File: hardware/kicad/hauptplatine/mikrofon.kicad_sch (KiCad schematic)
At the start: 20 parts, among them J601 Mikrofon, U601 TLV9001IDBVR

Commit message: update
Footprints BQ25185, Ra-01SH, DEGSON 15EDGRC-3.5 (2-6P) in Bienen.pretty; HW-02 Akkuhalter Keystone 1042 SMD; SCH26-13 Klemmen einreihig mit LCSC-Nummern. Tests: ERC 0, Pin/Footprint 0 Abweichungen, Netzprüfung 178/178, alle_tests_linux.sh rc=0
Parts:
- J601: footprint Connector_Phoenix_MC:PhoenixContact_MC_1,5_4-G-3.5_1x04_P3.50mm_Horizontal -> Bienen:DEGSON_15EDGRC-3.5-04P; LCSC (none) -> C7603438
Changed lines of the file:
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@@
 			)
 		)
-		(property "Footprint" "Connector_Phoenix_MC:PhoenixContact_MC_1,5_4-G-3.5_1x04_P3.50mm_Horizontal"
+		(property "Footprint" "Bienen:DEGSON_15EDGRC-3.5-04P"
 			(at 38.1 132.08 0)
 			(hide yes)
@@
 			)
 		)
-		(property "Description" "= J5 in anschluesse.md: 1 Schirm, 2 GND, 3 OUT, 4 VCC (3V3_ANA); DEGSON 15EDGRHC-3.5 4-polig C7603445 (Platzhalter-Footprint Phoenix MC) [P]; Schirm nur hier an Masse"
+		(property "Description" "= J5 in anschluesse.md: 1 Schirm, 2 GND, 3 OUT, 4 VCC (3V3_ANA); DEGSON 15EDGRC-3.5-04P; Schirm nur hier an Masse"
 			(at 38.1 132.08 0)
 			(hide yes)
+			(show_name no)
+			(do_not_autoplace no)
+			(effects
+				(font
+					(size 1.27 1.27)
+				)
+			)
+		)
+		(property "LCSC" "C7603438"
+			(at 38.1 132.08 0)
+			(hide yes)

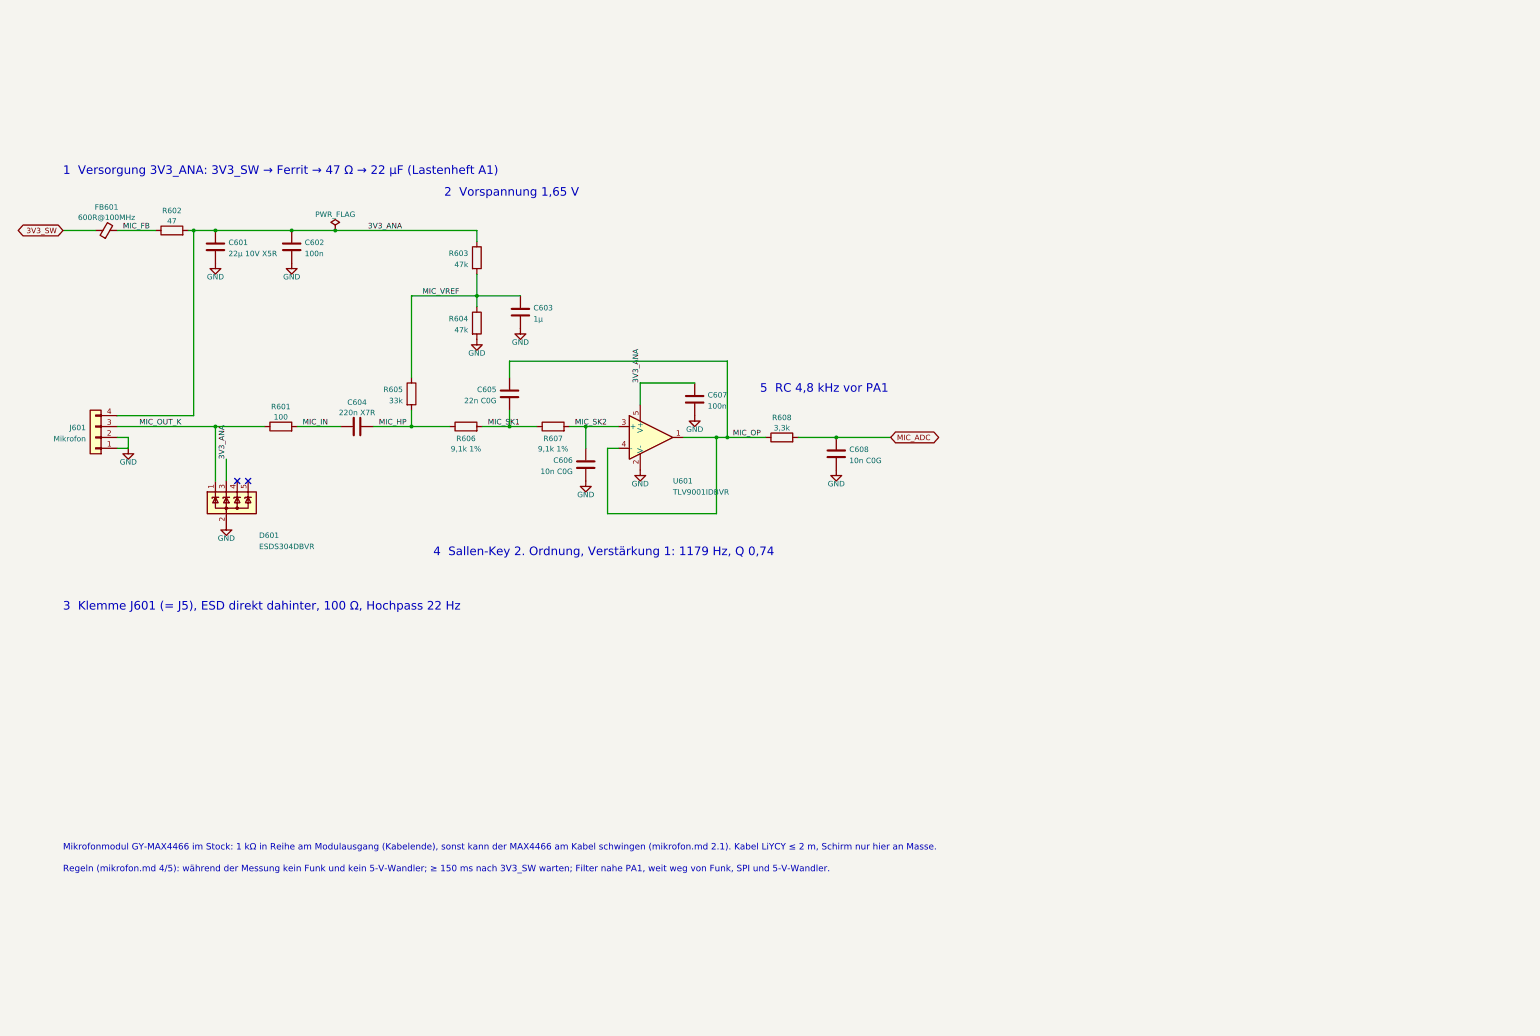
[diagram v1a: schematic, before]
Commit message: HW-07: zwei Mikrofone am Audio-ADC TLV320ADC3101, I2S3, RJ45 J5; HW-08: Platine nur Rahmen, Layout extern; Pflichtenheft und Übergabepaket für den Layouter; ERC 0, Netzprüfung 187/187, Pin/Footprint 0
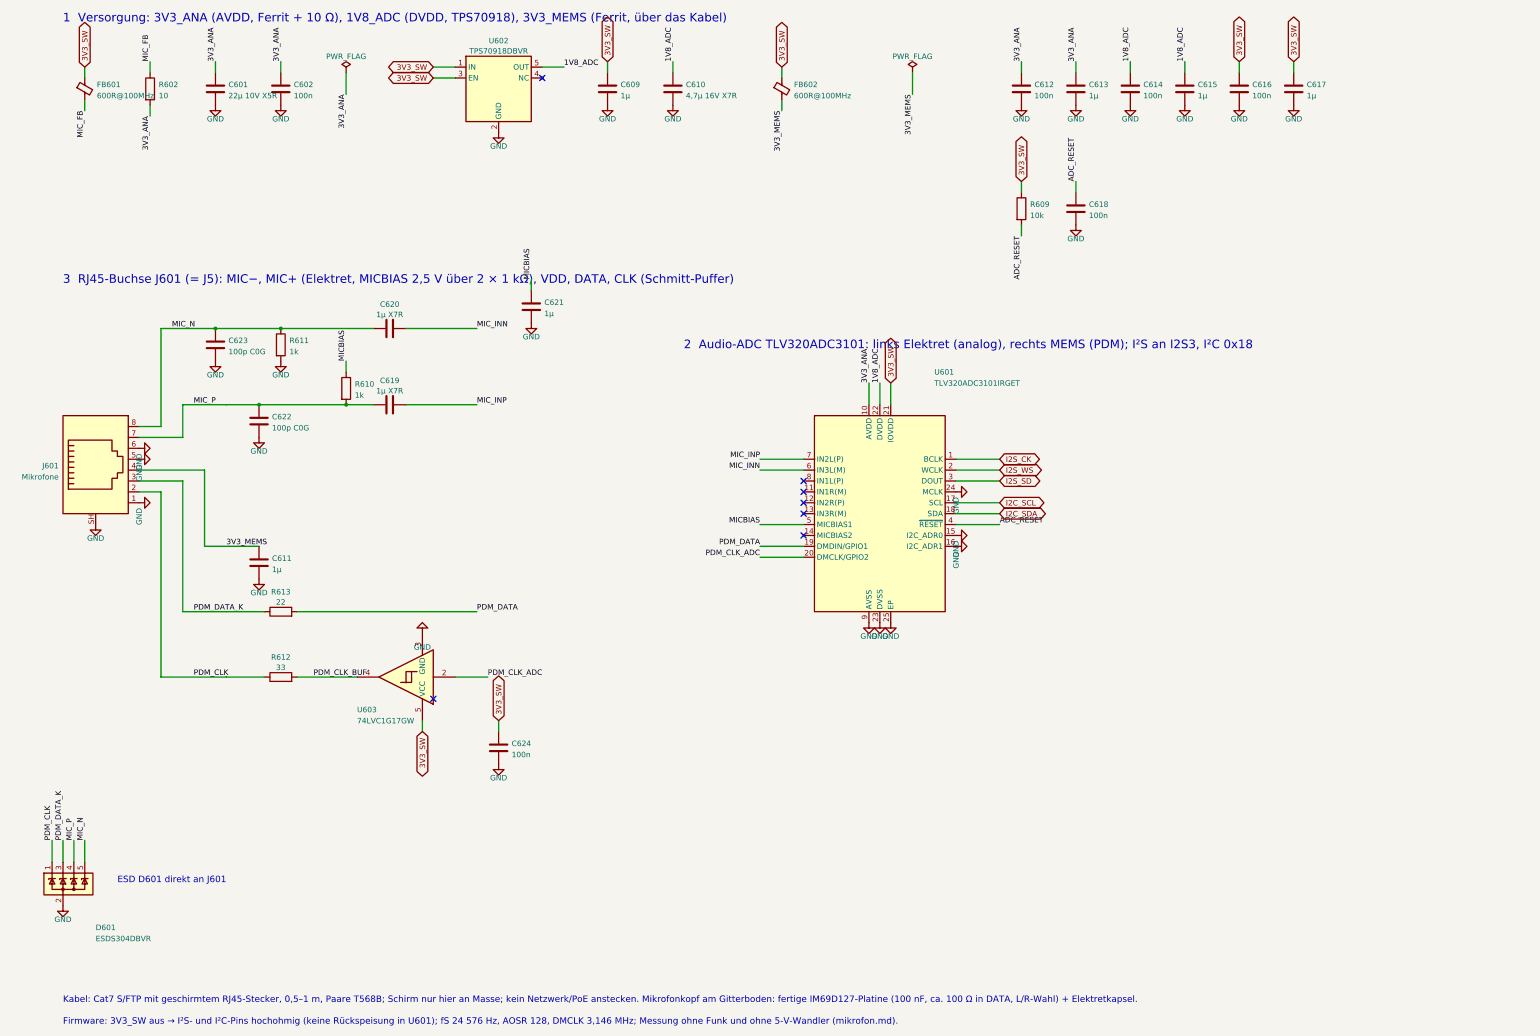
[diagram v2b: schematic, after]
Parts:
- removed C603: 1µ, Capacitor_SMD:C_0603_1608Metric, symbol Device:C
- removed C604: 220n X7R, Capacitor_SMD:C_0603_1608Metric, symbol Device:C
- removed C605: 22n C0G, Capacitor_SMD:C_0603_1608Metric, symbol Device:C
- removed C606, C608: 10n C0G, Capacitor_SMD:C_0603_1608Metric, symbol Device:C
- removed C607: 100n, Capacitor_SMD:C_0603_1608Metric, symbol Device:C
- removed R601: 100, Resistor_SMD:R_0603_1608Metric, symbol Device:R
- removed R603, R604: 47k, Resistor_SMD:R_0603_1608Metric, symbol Device:R
- removed R605: 33k, Resistor_SMD:R_0603_1608Metric, symbol Device:R
- removed R606, R607: 9,1k 1%, Resistor_SMD:R_0603_1608Metric, symbol Device:R
- removed R608: 3,3k, Resistor_SMD:R_0603_1608Metric, symbol Device:R
- added C609, C611, C613, C615, C617, C621: 1µ, Capacitor_SMD:C_0603_1608Metric, symbol Device:C
- added C610: 4,7µ 16V X7R, Capacitor_SMD:C_0805_2012Metric, symbol Device:C
- added C612, C614, C616, C618, C624: 100n, Capacitor_SMD:C_0603_1608Metric, symbol Device:C
- added C619, C620: 1µ X7R, Capacitor_SMD:C_0603_1608Metric, symbol Device:C
- added C622, C623: 100p C0G, Capacitor_SMD:C_0603_1608Metric, symbol Device:C
- added FB602: 600R@100MHz, Inductor_SMD:L_0603_1608Metric, symbol Device:FerriteBead_Small
- added R609: 10k, Resistor_SMD:R_0603_1608Metric, symbol Device:R
- added R610, R611: 1k, Resistor_SMD:R_0603_1608Metric, symbol Device:R
- added R612: 33, Resistor_SMD:R_0603_1608Metric, symbol Device:R
- added R613: 22, Resistor_SMD:R_0603_1608Metric, symbol Device:R
- added U602: TPS70918DBVR, Package_TO_SOT_SMD:SOT-23-5, symbol Bienen:TPS70933DBV
- added U603: 74LVC1G17GW, Package_TO_SOT_SMD:SOT-353_SC-70-5, symbol 74xGxx:74LVC1G17
- J601: value Mikrofon -> Mikrofone; footprint Bienen:DEGSON_15EDGRC-3.5-04P -> Connector_RJ:RJ45_RCH_RC01937; symbol Connector_Generic:Conn_01x04 -> Connector:RJ45_Shielded; LCSC C7603438 -> (none)
- R602: value 47 -> 10
- U601: value TLV9001IDBVR -> TLV320ADC3101IRGET; footprint Package_TO_SOT_SMD:SOT-23-5 -> Package_DFN_QFN:VQFN-24-1EP_4x4mm_P0.5mm_EP2.45x2.45mm; symbol Amplifier_Operational:MCP6001-OT -> Bienen:TLV320ADC3101; LCSC C398363 -> (none)
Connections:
- net 3V3_ANA: now also U601.10 (AVDD), C612.1, C613.1; no longer D601.3 (K), J601.4 (Pin_4), U601.5 (V+)
- net 3V3_SW: now also U601.21 (IOVDD), C609.1, C616.1, C617.1, C624.1, FB602.1, R609.1, U602.1 (IN), U602.3 (EN), U603.5 (VCC)
- net GND: now also J601.5, J601.6, J601.SH, U601.15 (I2C_ADR0), U601.16 (I2C_ADR1), U601.23 (DVSS), U601.24 (MCLK), U601.25 (EP), U601.9 (AVSS), C609.2, C610.2, C611.2, C612.2, C613.2, C614.2, C615.2, C616.2, C617.2, C618.2, C621.2, C622.2, C623.2, C624.2, R611.2, U602.2 (GND), U603.3 (GND); no longer J601.2 (Pin_2), U601.2 (V-)
- net MIC_P: now reaches D601.4 (K)
- net MIC_P: now also J601.7, C619.1, C622.1, R610.2
- net MIC_N: now reaches D601.5 (K)
- net MIC_N: now also J601.8, C620.1, C623.1, R611.1
- net MIC_OP renamed ADC_RESET
- net ADC_RESET: now also C618.1, R609.2; no longer U601.1
- net MIC_OUT_K renamed PDM_CLK
- net PDM_CLK: now also J601.2, R612.1; no longer J601.3 (Pin_3)
- net MIC_SK2 renamed I2S_SD
- new net 1V8_ADC: C610.1, C614.1, C615.1, U601.22 (DVDD), U602.5 (OUT)
- new net 3V3_MEMS: C611.1, FB602.2, J601.4
- new net I2C_SCL: U601.17 (SCL)
- new net I2C_SDA: U601.18 (SDA)
- new net I2S_CK: U601.1 (BCLK)
- new net I2S_WS: U601.2 (WCLK)
- new net MICBIAS: C621.1, R610.1, U601.5 (MICBIAS1)
- new net MIC_INN: C620.2, U601.6 (IN3L(M))
- new net MIC_INP: C619.2, U601.7 (IN2L(P))
- new net PDM_CLK_ADC: U601.20 (DMCLK/GPIO2), U603.2
- new net PDM_CLK_BUF: R612.2, U603.4
- new net PDM_DATA: R613.2, U601.19 (DMDIN/GPIO1)
- new net PDM_DATA_K: D601.3 (K), J601.3, R613.1
- no-connect marks 2 -> 7
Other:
- note added: "1 Versorgung: 3V3_ANA (AVDD, Ferrit + 10 Ω), 1V8_ADC (DVDD, TPS70918), 3V3_MEMS (Ferrit, über das Kabel)"
- note added: "2 Audio-ADC TLV320ADC3101: links Elektret (analog), rechts MEMS (PDM); I²S an I2S3, I²C 0x18"
- note added: "3 RJ45-Buchse J601 (= J5): MIC−, MIC+ (Elektret, MICBIAS 2,5 V über 2 × 1 kΩ), VDD, DATA, CLK (Schmitt-Puffer)"
- note added: "ESD D601 direkt an J601"
- note added: "Firmware: 3V3_SW aus → I²S- und I²C-Pins hochohmig (keine Rückspeisung in U601); fS 24 576 Hz, AOSR 128, DMCLK 3,146 MHz; Messung ohne Funk und ohne 5-V-Wandler (mikrofon.md)."
- note added: "Kabel: Cat7 S/FTP mit geschirmtem RJ45-Stecker, 0,5–1 m, Paare T568B; Schirm nur hier an Masse; kein Netzwerk/PoE anstecken. Mikrofonkopf am Gitterboden: fertige IM69D127-Platine (100 nF, ca. 100 Ω in DATA, L/R-Wahl) + Elektretkapsel."
- note removed: "1 Versorgung 3V3_ANA: 3V3_SW → Ferrit → 47 Ω → 22 µF (Lastenheft A1)"
- note removed: "2 Vorspannung 1,65 V"
- note removed: "3 Klemme J601 (= J5), ESD direkt dahinter, 100 Ω, Hochpass 22 Hz"
- note removed: "4 Sallen-Key 2. Ordnung, Verstärkung 1: 1179 Hz, Q 0,74"
- note removed: "5 RC 4,8 kHz vor PA1"
- note removed: "Mikrofonmodul GY-MAX4466 im Stock: 1 kΩ in Reihe am Modulausgang (Kabelende), sonst kann der MAX4466 am Kabel schwingen (mikrofon.md 2.1). Kabel LiYCY ≤ 2 m, Schirm nur hier an Masse."
- note removed: "Regeln (mikrofon.md 4/5): während der Messung kein Funk und kein 5-V-Wandler; ≥ 150 ms nach 3V3_SW warten; Filter nahe PA1, weit weg von Funk, SPI und 5-V-Wandler."
- title: Mikrofon: 3V3_ANA, Hochpass, Sallen-Key 1,18 kHz, ADC-Eingang PA1 -> Mikrofon: Audio-ADC TLV320ADC3101, Elektret (analog) + MEMS IM69D127 (PDM), I²S an I2S3
- moved on the sheet: C601, C602, D601, FB601, R602
